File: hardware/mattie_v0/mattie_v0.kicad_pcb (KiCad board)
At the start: 4 copper layers, 55 x 32 mm, 52 parts, among them J1 5V, J2 USB_B_Mini, J3 Power, U1 STM32F40X_LQFP64, U2 ICE40UP5K-SG48ITR, U3 MCP1826T, U4 MCP1826S-3302, U5 DSC1004, Y1 8Mhz

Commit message: routing
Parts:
- moved C22 2.04 mm to (163.4, 133.5), turned to 270 degrees
- moved C18 1.73 mm to (168.1, 124.6)
- moved C23 1.11 mm to (175.4, 133.9), turned to 0 degrees
- moved C2 0.85 mm to (163.4, 130.5)
- moved U5 0.80 mm to (172.2, 125.7)
- moved C21 0.17 mm to (166.6, 130.0)
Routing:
- net GND: track 203.5 -> 363.8 mm, vias 13 -> 46
- net +3V3: track 118.0 -> 194.3 mm, vias 4 -> 11
- net /LATTICE_ICE40/DAT5: track 0.00 -> 35.1 mm, vias 0 -> 2
- net /MCU/LED_RED: track 0.00 -> 35.0 mm, vias 0 -> 3
- net /LATTICE_ICE40/DAT14: track 0.00 -> 32.9 mm, vias 0 -> 2
- net /MCU/NRST: track 0.00 -> 29.7 mm, vias 0 -> 1
- net /LATTICE_ICE40/DAT12: track 0.00 -> 29.0 mm, vias 0 -> 2
- net /LATTICE_ICE40/DAT15: track 0.00 -> 28.8 mm, vias 0 -> 2
- net /LATTICE_ICE40/DAT13: track 0.00 -> 28.3 mm, vias 0 -> 2
- net /LATTICE_ICE40/AUX2: track 0.00 -> 28.2 mm, vias 0 -> 3
- net /LATTICE_ICE40/DAT7: track 0.00 -> 26.9 mm, vias 0 -> 2
- net /LATTICE_ICE40/AUX5: track 0.00 -> 26.8 mm, vias 0 -> 2
- net /LATTICE_ICE40/AUX4: track 0.00 -> 25.6 mm, vias 0 -> 3
- net /LATTICE_ICE40/SPI_MOSI: track 0.00 -> 24.3 mm, vias 0 -> 2
- net /LATTICE_ICE40/DAT4: track 0.00 -> 23.8 mm, vias 0 -> 2
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- added copper zone on B.Cu, net GND
- added copper zone on In1.Cu, net GND
- added copper zone on In2.Cu, net GND

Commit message: tweaking and cleaning
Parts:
- 5 - 6V: renamed from J1
- renumbered J3 to POWER
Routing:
- net GND: track 363.8 -> 399.6 mm, vias 46 -> 52
- net +3V3: track 194.3 -> 188.2 mm, vias 11 -> 10
- net /LATTICE_ICE40/DAT2: track 21.8 -> 26.7 mm
- net /LATTICE_ICE40/DAT1: track 18.2 -> 22.8 mm
- net /DCDC/5V: track 50.3 -> 46.5 mm, vias 5 -> 0
- net /LATTICE_ICE40/DAT3: track 21.9 -> 25.5 mm
- net /LATTICE_ICE40/SPI_SCK: track 21.1 -> 19.3 mm
- net +1V2: track 77.4 -> 75.5 mm
- net /LATTICE_ICE40/DAT6: track 23.5 -> 21.9 mm
- net /LATTICE_ICE40/DAT14: track 32.9 -> 31.7 mm
- net /LATTICE_ICE40/DAT4: track 23.8 -> 22.7 mm
- net /LATTICE_ICE40/DAT7: track 26.9 -> 25.9 mm
- net /MCU/LED_YELLOW: track 14.9 -> 15.9 mm
- net /LATTICE_ICE40/DAT12: track 29.0 -> 29.8 mm
- net /LATTICE_ICE40/SPI_MISO: track 19.7 -> 19.0 mm
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- removed copper zone on F.Cu, net /DCDC/5V
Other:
- board text added: "+"
- board text added: "B"
- board text added: "GND"
- board text added: "MATTIE"
- board text added: "N"
- board text removed: "MATTIE V0"

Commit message: tweaks
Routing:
- net GND: track 399.6 -> 428.7 mm, vias 52 -> 57
- net /MCU/GPIO5: track 20.6 -> 37.2 mm
- net /MCU/GPIO7: track 18.2 -> 32.8 mm
- net /MCU/GPIO6: track 20.2 -> 33.9 mm
- net +3V3: track 188.2 -> 200.6 mm
- net /LATTICE_ICE40/SPI_SS: track 18.8 -> 13.5 mm, vias 2 -> 0
- net /MCU/SWCLK: track 19.3 -> 15.4 mm, vias 2 -> 1
- net /LATTICE_ICE40/DAT12: track 29.8 -> 32.6 mm
- net /LATTICE_ICE40/AUX3: track 22.3 -> 19.6 mm
- net /DCDC/REG1V2_ON: track 22.8 -> 20.8 mm, vias 3 -> 2
- net /LATTICE_ICE40/DAT2: track 26.7 -> 28.6 mm
- net /LATTICE_ICE40/AUX2: track 28.2 -> 29.8 mm
- net /LATTICE_ICE40/DAT3: track 25.5 -> 27.0 mm
- net /LATTICE_ICE40/RESET: track 12.2 -> 10.7 mm
- net Net-(R5-Pad1): track 12.9 -> 14.4 mm
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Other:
- rule pad_to_mask_clearance: 0.051 -> 0.02
- rule solder_mask_min_width: 0.25 -> 0.04
- board text added: "*"
- board text added: "1"
- board text added: "11"
- board text added: "12"
- board text added: "1V2"
- board text added: "2"
- board text added: "3V3"
- board text added: "5 - 6V"
- board text added: "7"
- board text added: "8"
- board text added: "GPIO"
- board text added: "MATTIE V0 Bo Joel Svensson Marvin Damschen"
- board text added: "NRST"
- board text added: "SWCLK"
- board text added: "SWDIO"

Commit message: tweaks
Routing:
- net GND: track 428.7 -> 447.0 mm, vias 57 -> 56
- net /MCU/NRST: track 28.6 -> 29.6 mm, vias 1 -> 3
- net /LATTICE_ICE40/DAT11: track 16.3 -> 17.2 mm
- net /LATTICE_ICE40/DAT5: track 34.0 -> 33.3 mm
- net /LATTICE_ICE40/DAT10: track 18.9 -> 19.4 mm

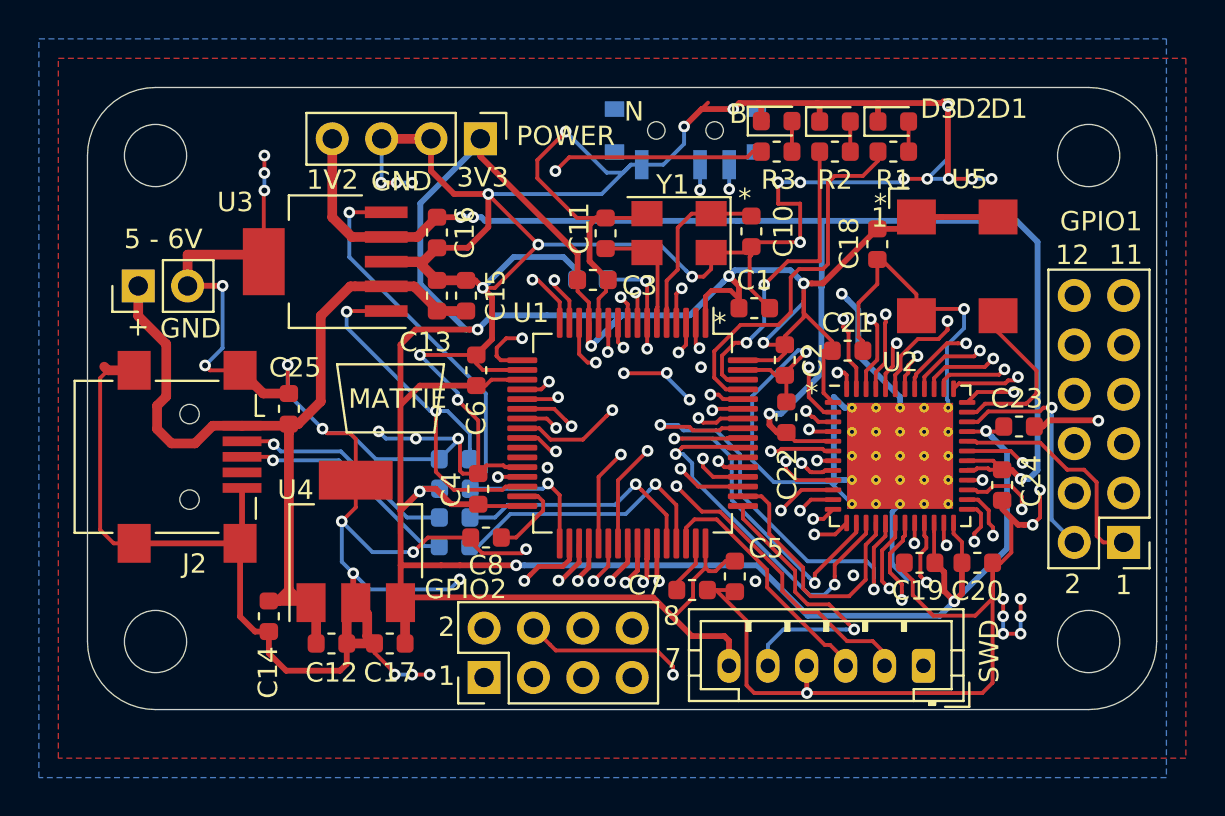
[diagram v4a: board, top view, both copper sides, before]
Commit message: added powerswitch for USB power
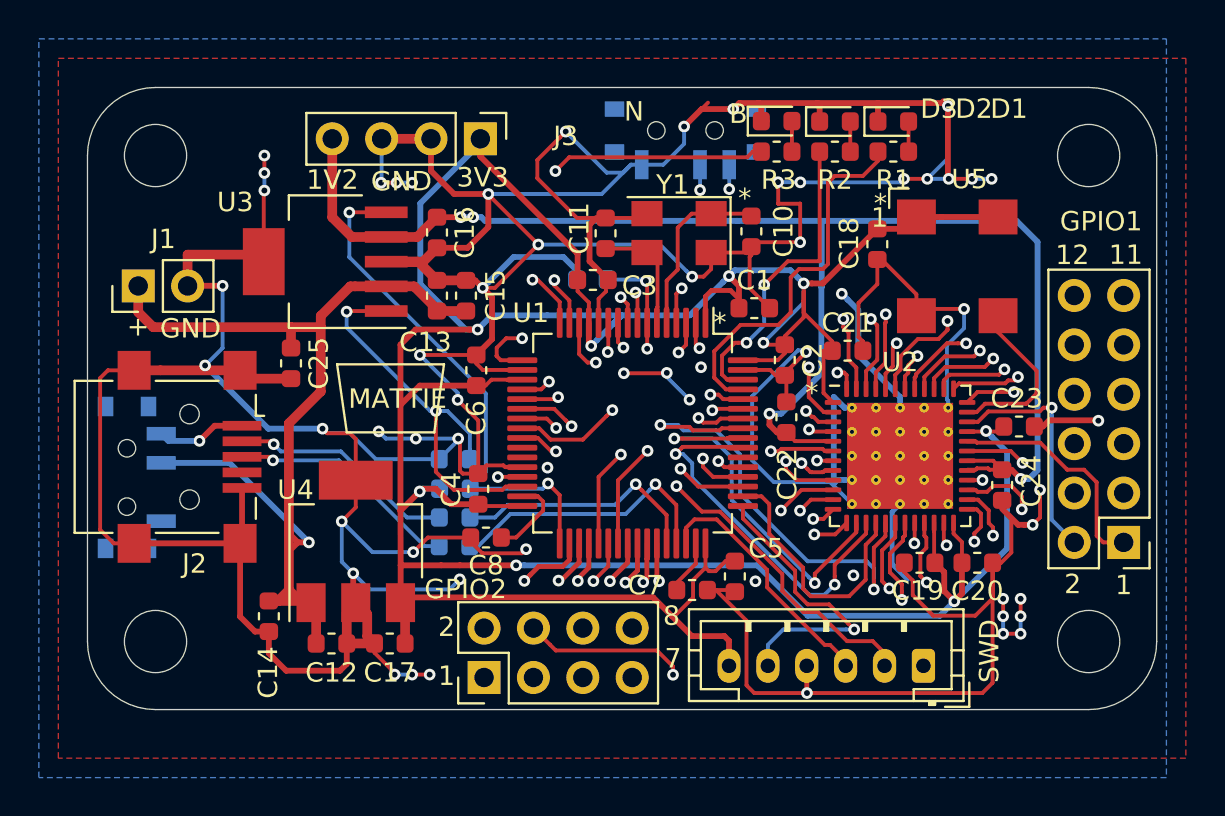
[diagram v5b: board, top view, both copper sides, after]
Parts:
- added USB_POWER: USB_POWER, Button_Switch_SMD:SW_SPDT_PCM12, B.Cu at (129.9, 136.6)
- J1: renamed from 5 - 6V
- moved C25 2.34 mm to (138.0, 130.7), turned to 270 degrees
- renumbered BOOT to BOOT_MODE, POWER to J3
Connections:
- C12 pad 1: /DCDC/5V -> /DCDC/5V_IN
- C13 pad 1: /DCDC/5V -> /DCDC/5V_IN
- C14 pad 1: /DCDC/5V -> /DCDC/5V_IN
- C15 pad 1: /DCDC/5V -> /DCDC/5V_IN
- C25 pad 1: /DCDC/5V -> /DCDC/5V_IN
- J1 pad 1: /DCDC/5V -> /DCDC/5V_IN
- U3 pad 2: /DCDC/5V -> /DCDC/5V_IN
- U4 pad 1: /DCDC/5V -> /DCDC/5V_IN
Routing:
- net /DCDC/5V_IN: track 0.00 -> 55.9 mm, vias 0 -> 1
- net /DCDC/5V: track 46.5 -> 4.64 mm, vias 0 -> 1
- net GND: track 447.0 -> 453.9 mm, vias 56 -> 55
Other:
- board text added: "EXT_POWER"
- board text added: "OFF"
- board text added: "ON"
